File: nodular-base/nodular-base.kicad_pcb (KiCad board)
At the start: 4 copper layers, 83.1 x 92.5 mm, 184 parts, among them J1 Conn_02x10_Counter_Clockwise, J10 Conn_01x02_MountingPin, J11 Conn_01x08_Pin, J2 Conn_02x10_Counter_Clockwise, J3 Conn_02x10_Counter_Clockwise, J4 Conn_02x10_Counter_Clockwise, J5 Conn_02x10_Counter_Clockwise, J6 Conn_02x10_Counter_Clockwise, J7 USB_C_Receptacle_USB2.0, J8 USB_C_Receptacle_USB2.0, J9 Conn_01x30_MountingPin, SW1 SW_Push, SW2 SW_Push, SW3 SW_Push, U1 ESP32-S3-PICO-1-N8R2, U10 MT9700, U11 MT9700, U12 MT9700, U13 MT9700, U14 MT9700, U15 74LVC1G04, U16 RCLAMP0524P-ES, U17 RCLAMP0524P-ES, U18 RCLAMP0524P-ES, U19 74LVC1G04, U2 FUSB302BMPX, U20 RCLAMP0524P-ES, U21 RCLAMP0524P-ES, U22 RCLAMP0524P-ES, U23 74LVC1G04, U24 AW9523B, U25 AW9523B, U26 AW9523B, U27 RCLAMP0524P-ES, U28 RCLAMP0524P-ES, U29 RCLAMP0524P-ES, U3 BQ25895RTW, U30 RCLAMP0524P-ES, U31 74LVC1G04, U32 74LVC1G04, U33 74LVC1G04, U34 RCLAMP0524P-ES, U35 RCLAMP0524P-ES, U36 RCLAMP0524P-ES, U37 RCLAMP0524P-ES, U38 RCLAMP0524P-ES, U39 RCLAMP0524P-ES, U4 TCA9548APWR, U40 RCLAMP0524P-ES, U41 RCLAMP0524P-ES, U42 RCLAMP0524P-ES, U43 TLV62595DMQR, U44 RCLAMP0524P-ES, U45 RCLAMP0524P-ES, U46 RCLAMP0524P-ES, U47 RCLAMP0524P-ES, U48 RCLAMP0524P-ES, U49 RCLAMP0524P-ES, U5 FUSB302BMPX, U50 TS3USB221A, U51 MT9700, U6 74LVC1G17, U7 SC7A20, U8 MT9700, U9 MT9700

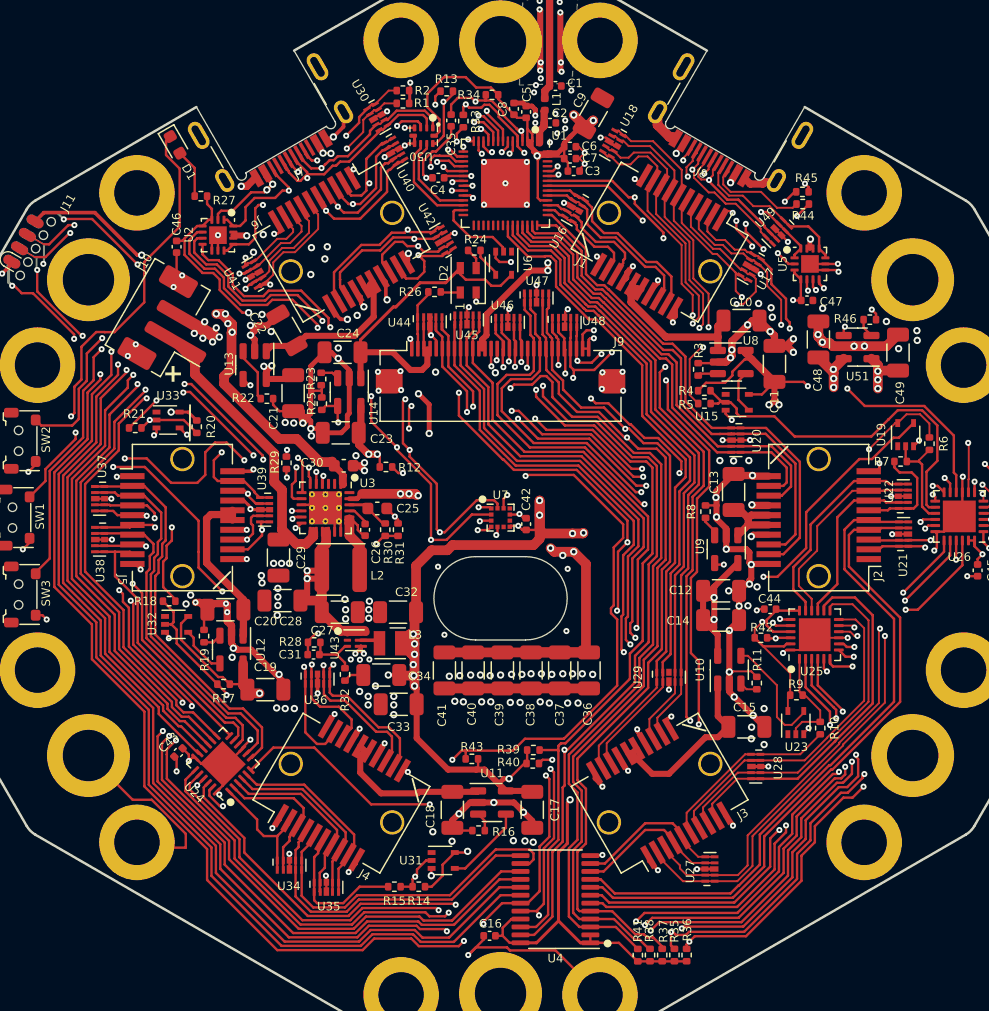
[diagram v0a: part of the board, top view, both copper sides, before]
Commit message: Add 3d models and fix erc errors
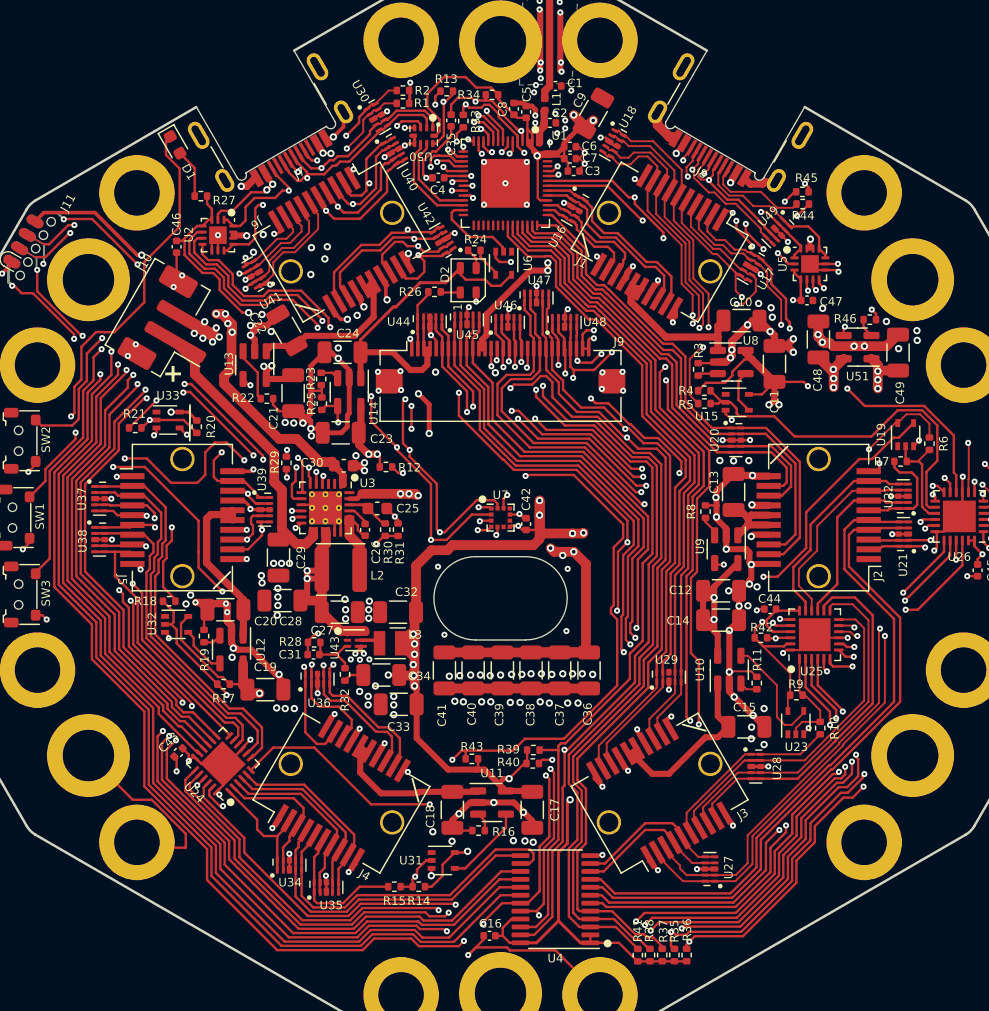
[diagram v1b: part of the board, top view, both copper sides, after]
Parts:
- D2: footprint LED_SMD:LED_SK6805_PLCC4_2.4x2.7mm_P1.3mm -> nodular:LED_SK6805_PLCC4_2.4x2.7mm_P1.3mm
- U16, U17, U18, U20, U21, U22, U27, U28, U29, U30, U34, U35, U36, U37, U38, U39, U40, U41, U42, U44, U45, U46, U47, U48, U49: footprint Package_DFN_QFN:Diodes_UDFN-10_1.0x2.5mm_P0.5mm -> nodular:Diodes_UDFN-10_1.0x2.5mm_P0.5mm

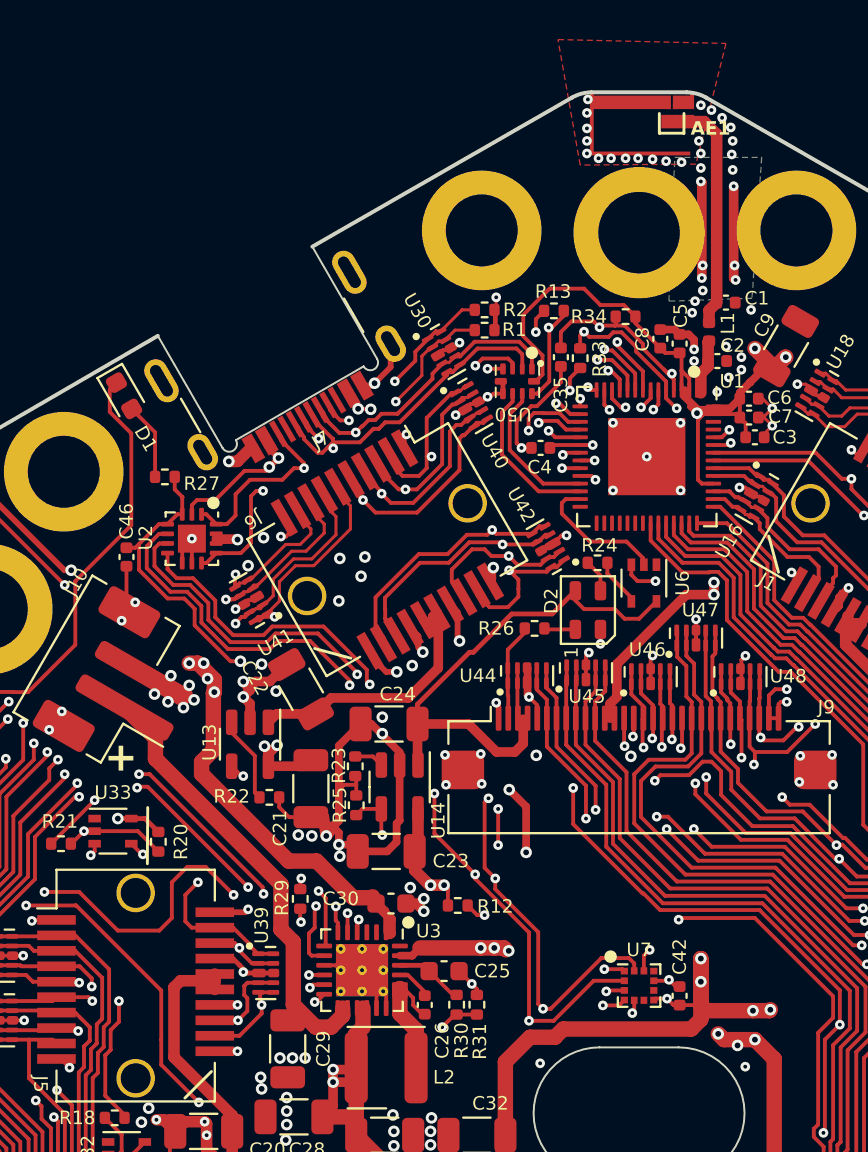
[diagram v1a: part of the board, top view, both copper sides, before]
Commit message: Increase width of high current traces, make antenna trace closer to 50 ohm, add vias to sides of antenna trace
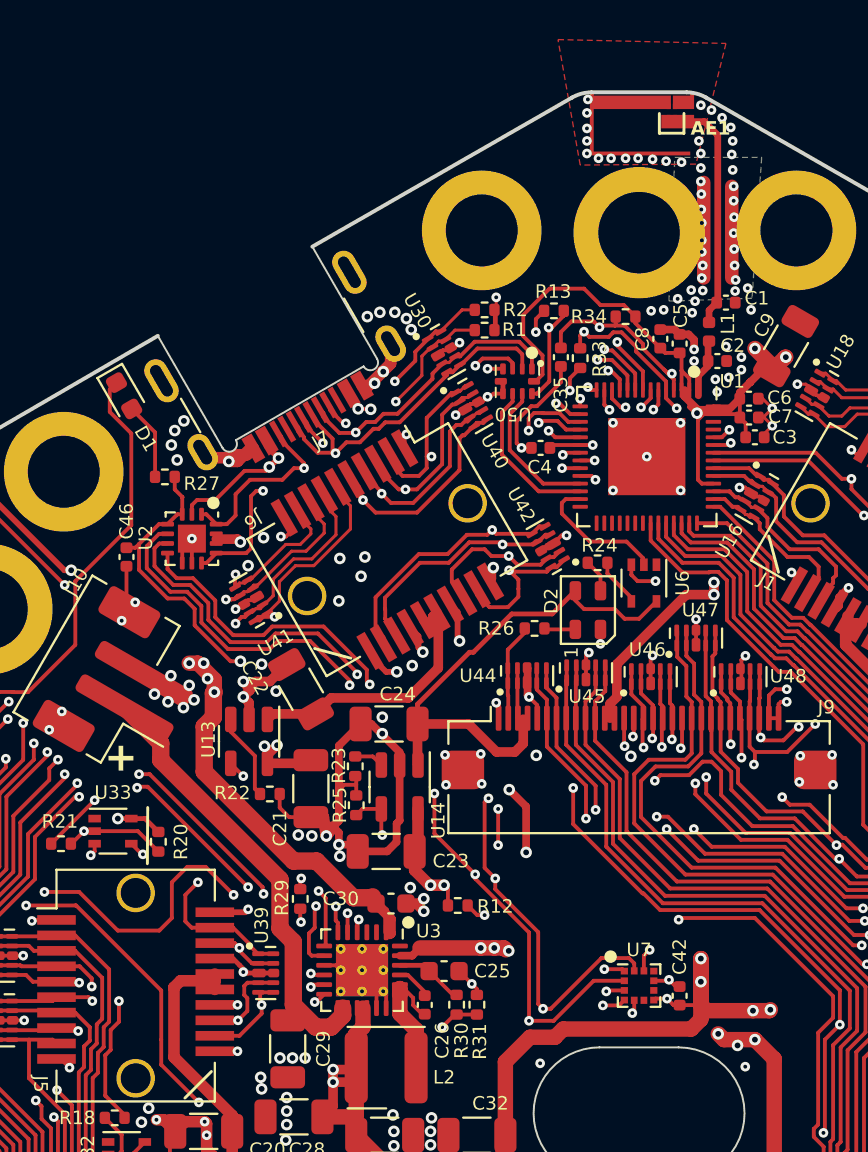
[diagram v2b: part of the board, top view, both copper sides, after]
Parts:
- moved R22 0.18 mm to (80.9, 90.1)
- moved U13 0.16 mm to (79.8, 87.3)
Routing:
- net GND: track 362.7 -> 368.7 mm, vias 302 -> 328
- net /DEV_USB+: track 45.2 -> 45.8 mm

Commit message: Add labels to baseboard
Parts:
- added kibuzzard-657A1FC2: G***, kibuzzard-657A1FC2, B.Cu at (116.0, 73.0)
- added kibuzzard-657A1FCE: G***, kibuzzard-657A1FCE, B.Cu at (84.1, 72.6)
- added kibuzzard-657A201C: G***, kibuzzard-657A201C, B.Cu at (61.9, 93.8)
- added kibuzzard-657A2038: G***, kibuzzard-657A2038, B.Cu at (61.3, 100.1)
- added kibuzzard-657A2068: G***, kibuzzard-657A2068, B.Cu at (61.9, 106.3)
